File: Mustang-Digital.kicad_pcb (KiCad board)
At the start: 4 copper layers, 67 x 105.4 mm, 117 parts, among them J1 685119248123, J2 685119248123, J3 Conn_01x02_Pin, J303 2130830005, J4 Micro_SD_Card_4.0_CUI, U1 BM83SM1-00TB, U2 LP5012RUKR, U3 STM32L496VGTx, U301 SPU03L-05, U302 SPU03L-05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

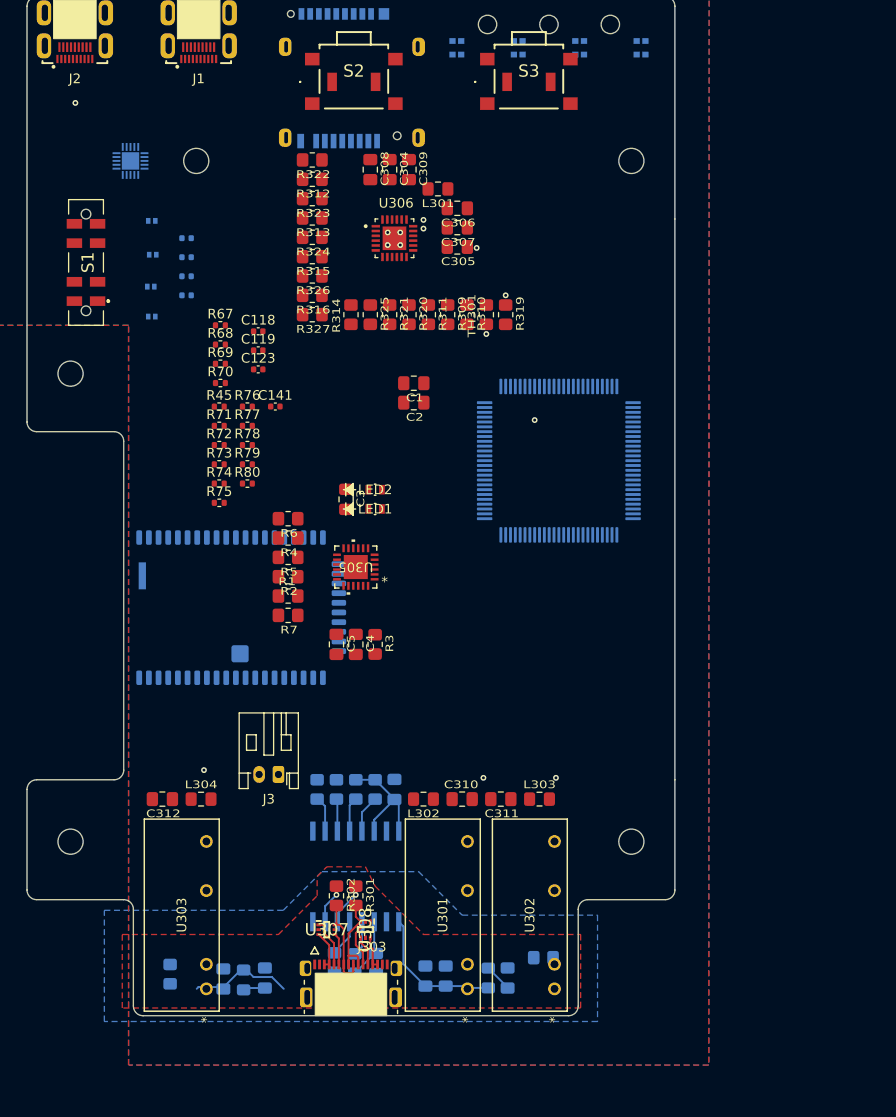
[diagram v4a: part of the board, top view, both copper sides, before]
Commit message: Electrical Rules Check fixes in progress.
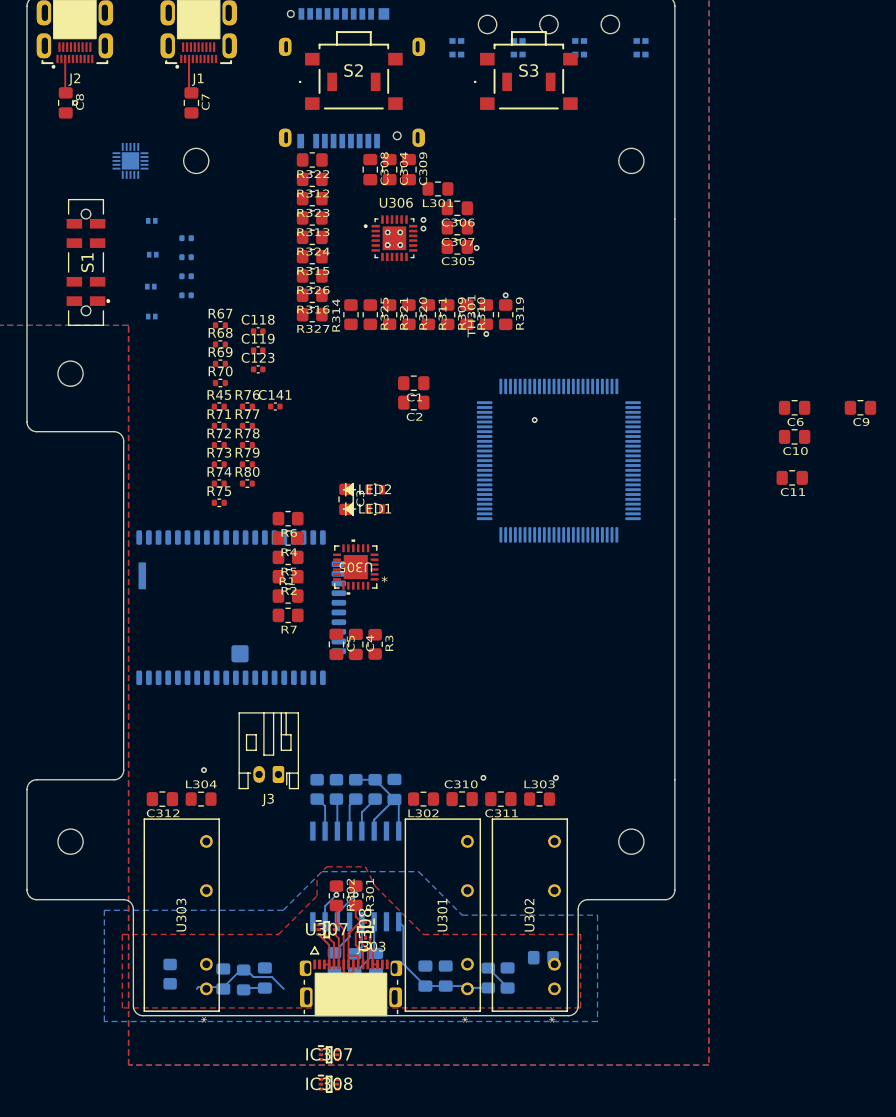
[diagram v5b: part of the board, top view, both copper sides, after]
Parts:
- added C10: 0.1uF, Mustang_Library:C_0805_2012Metric_Pad1.18x1.45mm_HandSolder, F.Cu at (169.4, 85.5)
- added C11: 0.1uF, Mustang_Library:C_0805_2012Metric_Pad1.18x1.45mm_HandSolder, F.Cu at (169.1, 89.8)
- added C6: 0.1uF, Mustang_Library:C_0805_2012Metric_Pad1.18x1.45mm_HandSolder, F.Cu at (169.4, 82.5)
- added C7: 0.1uF, Mustang_Library:C_0805_2012Metric_Pad1.18x1.45mm_HandSolder, F.Cu at (107.0, 51.0)
- added C8: 0.1uF, Mustang_Library:C_0805_2012Metric_Pad1.18x1.45mm_HandSolder, F.Cu at (94.0, 51.0)
- added C9: 0.1uF, Mustang_Library:C_0805_2012Metric_Pad1.18x1.45mm_HandSolder, F.Cu at (176.2, 82.5)
- added IC307: TPD4E1B06DRLR, Mustang_Library:SOTFL50P160X60-6N, F.Cu at (121.2, 149.4)
- added IC308: TPD4E1B06DRLR, Mustang_Library:SOTFL50P160X60-6N, F.Cu at (121.2, 152.5)
- J1, J2: value 685119248123 -> 685119248123_Left
- J3: value Conn_01x02_Pin -> Conn_01x02_Pin_JST-PH_Batt
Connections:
- net /Charging_Isolation/VBUS-ISO renamed /Charging_Isolation/5V
- net BT_PAIR renamed Net-(S1-NO_3)
- net LEDSCL renamed /LEDS_BUTTONS_SWITCHES/LED_SCL
- net LEDSDA renamed /LEDS_BUTTONS_SWITCHES/LED_SDA
- net LED_EN renamed /LEDS_BUTTONS_SWITCHES/LED_EN
- net MCU_PWR renamed Net-(S1-NC_1)
- net MCU_Record renamed /LEDS_BUTTONS_SWITCHES/SW_RECORD
- net Net-(C144-Pad2) renamed /LEDS_BUTTONS_SWITCHES/SW_PWR
- net Net-(C145-Pad2) renamed /LEDS_BUTTONS_SWITCHES/SW_BTPAIR
- net TOMCUGPIO renamed /LEDS_BUTTONS_SWITCHES/SW_PLAY
- C1 pad 1: /Charging_Isolation/3V3 -> +3V3
- C2 pad 1: /Charging_Isolation/3V3 -> +3V3
- C303 pad 2: /Charging_Isolation/3V3 -> +3V3
- J1 pad 1: unconnected-(J1-Pad1) -> /Buds/SPK_AUDIO+L
- J1 pad 10: unconnected-(J1-Pad10) -> GND
- J1 pad 11: unconnected-(J1-Pad11) -> /Buds/I2C_SCL
- J1 pad 12: unconnected-(J1-Pad12) -> /Buds/SPI_MISOL
- J1 pad 13: unconnected-(J1-Pad13) -> GND
- J1 pad 14: unconnected-(J1-Pad14) -> /Buds/SPI_CKL
- J1 pad 15: unconnected-(J1-Pad15) -> /Buds/SPI_MOSIL
- J1 pad 16: unconnected-(J1-Pad16) -> GND
- J1 pad 17: unconnected-(J1-Pad17) -> /Buds/SPI_CSL
- J1 pad 18: unconnected-(J1-Pad18) -> /Buds/ENABLE_PINS
- J1 pad 19: unconnected-(J1-Pad19) -> /Buds/ADS_DRDYL
- J1 pad 2: unconnected-(J1-Pad2) -> /Buds/SPK_AUDIO-L
- J1 pad 3: unconnected-(J1-Pad3) -> /Buds/REF
- J1 pad 4: unconnected-(J1-Pad4) -> GND
- J1 pad 5: unconnected-(J1-Pad5) -> /Buds/VSYS
- J1 pad 6: unconnected-(J1-Pad6) -> /Buds/TALK_MICL
- J1 pad 7: unconnected-(J1-Pad7) -> GND
- J1 pad 8: unconnected-(J1-Pad8) -> /Buds/IMU_CSL
- J1 pad 9: unconnected-(J1-Pad9) -> /Buds/I2C_SDA
- J1 pad S1: GND -> Net-(J1-SHIELD-PadS1)
- J1 pad S2: GND -> Net-(J1-SHIELD-PadS1)
- J1 pad S3: GND -> Net-(J1-SHIELD-PadS1)
- J1 pad S4: GND -> Net-(J1-SHIELD-PadS1)
- J2 pad 1: unconnected-(J2-Pad1) -> /Buds/SPK_AUDIO+R
- J2 pad 10: unconnected-(J2-Pad10) -> GND
- J2 pad 11: unconnected-(J2-Pad11) -> /Buds/I2C_SCL
- J2 pad 12: unconnected-(J2-Pad12) -> /Buds/SPI_MISOR
- J2 pad 13: unconnected-(J2-Pad13) -> GND
- J2 pad 14: unconnected-(J2-Pad14) -> /Buds/SPI_CKR
- J2 pad 15: unconnected-(J2-Pad15) -> /Buds/SPI_MOSIR
- J2 pad 16: unconnected-(J2-Pad16) -> GND
- J2 pad 17: unconnected-(J2-Pad17) -> /Buds/SPI_CSR
- J2 pad 18: unconnected-(J2-Pad18) -> /Buds/ENABLE_PINS
- J2 pad 19: unconnected-(J2-Pad19) -> /Buds/ADS_DRDYR
- J2 pad 2: unconnected-(J2-Pad2) -> /Buds/SPK_AUDIO-R
- J2 pad 3: unconnected-(J2-Pad3) -> /Buds/REF
- J2 pad 4: unconnected-(J2-Pad4) -> GND
- J2 pad 5: unconnected-(J2-Pad5) -> /Buds/VSYS
- J2 pad 6: unconnected-(J2-Pad6) -> /Buds/TALK_MICR
- J2 pad 7: unconnected-(J2-Pad7) -> GND
- J2 pad 8: unconnected-(J2-Pad8) -> /Buds/IMU_CSR
- J2 pad 9: unconnected-(J2-Pad9) -> /Buds/I2C_SDA
- J2 pad S1: GND -> Net-(J2-SHIELD-PadS1)
- J2 pad S2: GND -> Net-(J2-SHIELD-PadS1)
- J2 pad S3: GND -> Net-(J2-SHIELD-PadS1)
- J2 pad S4: GND -> Net-(J2-SHIELD-PadS1)
- J3 pad 1: /Charging_Isolation/BAT -> +BATT
- J3 pad 2: GND -> -BATT
- J303 pad SH1: GNDPWR -> Net-(J303-SHIELD1)
- J303 pad SH2: GNDPWR -> Net-(J303-SHIELD1)
- J303 pad SH3: GNDPWR -> Net-(J303-SHIELD1)
- J303 pad SH4: GNDPWR -> Net-(J303-SHIELD1)
- J4 pad 10: unconnected-(J4-SHIELD-Pad10) -> Net-(J4-SHIELD-Pad10)
- J4 pad 11: unconnected-(J4-SHIELD-Pad11) -> Net-(J4-SHIELD-Pad10)
- J4 pad 12: unconnected-(J4-SHIELD-Pad12) -> Net-(J4-SHIELD-Pad10)
- J4 pad 13: unconnected-(J4-SHIELD-Pad13) -> Net-(J4-SHIELD-Pad10)
- J4 pad 14: unconnected-(J4-SHIELD-Pad14) -> Net-(J4-SHIELD-Pad10)
- R312 pad 1: /Charging_Isolation/3V3 -> +3V3
- R313 pad 1: /Charging_Isolation/3V3 -> +3V3
- R314 pad 1: /Charging_Isolation/3V3 -> +3V3
- R315 pad 1: /Charging_Isolation/3V3 -> +3V3
- R315 pad 2: /Charging_Isolation/_SCL -> /Charging_Isolation/SCL
- R316 pad 1: /Charging_Isolation/3V3 -> +3V3
- R316 pad 2: /Charging_Isolation/_SDA -> /Charging_Isolation/SDA
- S3 pad MP1: unconnected-(S3-PadMP1) -> GND
- S3 pad MP2: unconnected-(S3-PadMP2) -> GND
- S3 pad MP3: unconnected-(S3-PadMP3) -> GND
- S3 pad MP4: unconnected-(S3-PadMP4) -> GND
- U2 pad 14: GND -> Net-(U2-ADDR0)
- U2 pad 15: GND -> Net-(U2-ADDR1)
- U304 pad 14: /Charging_Isolation/3V3 -> +3V3
- U304 pad 16: /Charging_Isolation/3V3 -> +3V3
- U305 pad 1: /Charging_Isolation/3V3 -> +3V3
- U305 pad 15: /Charging_Isolation/_RESET_N -> /Charging_Isolation/RESET_N
- U305 pad 18: /Charging_Isolation/3V3 -> +3V3
- U305 pad 9: /Charging_Isolation/3V3 -> +3V3
- U306 pad 5: /Charging_Isolation/_SCL -> /Charging_Isolation/SCL
- U306 pad 6: /Charging_Isolation/_SDA -> /Charging_Isolation/SDA
- U307 pad 5: /Charging_Isolation/NC307 -> GNDPWR
- U308 pad 5: /Charging_Isolation/NC308 -> GNDPWR
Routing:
- net Net-(J2-SHIELD-PadS1): track 0.00 -> 13.0 mm
- net Net-(J1-SHIELD-PadS1): track 0.00 -> 13.0 mm
- net /Buds/VSYS: track 0.00 -> 7.13 mm
